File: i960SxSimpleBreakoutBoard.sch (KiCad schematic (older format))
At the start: 24 parts, among them J1 Conn_01x18, J4 Conn_01x05, J5 Multiplexed Address/Data Lines, J6 Upper 16 Address Lines, U1 80960Sx

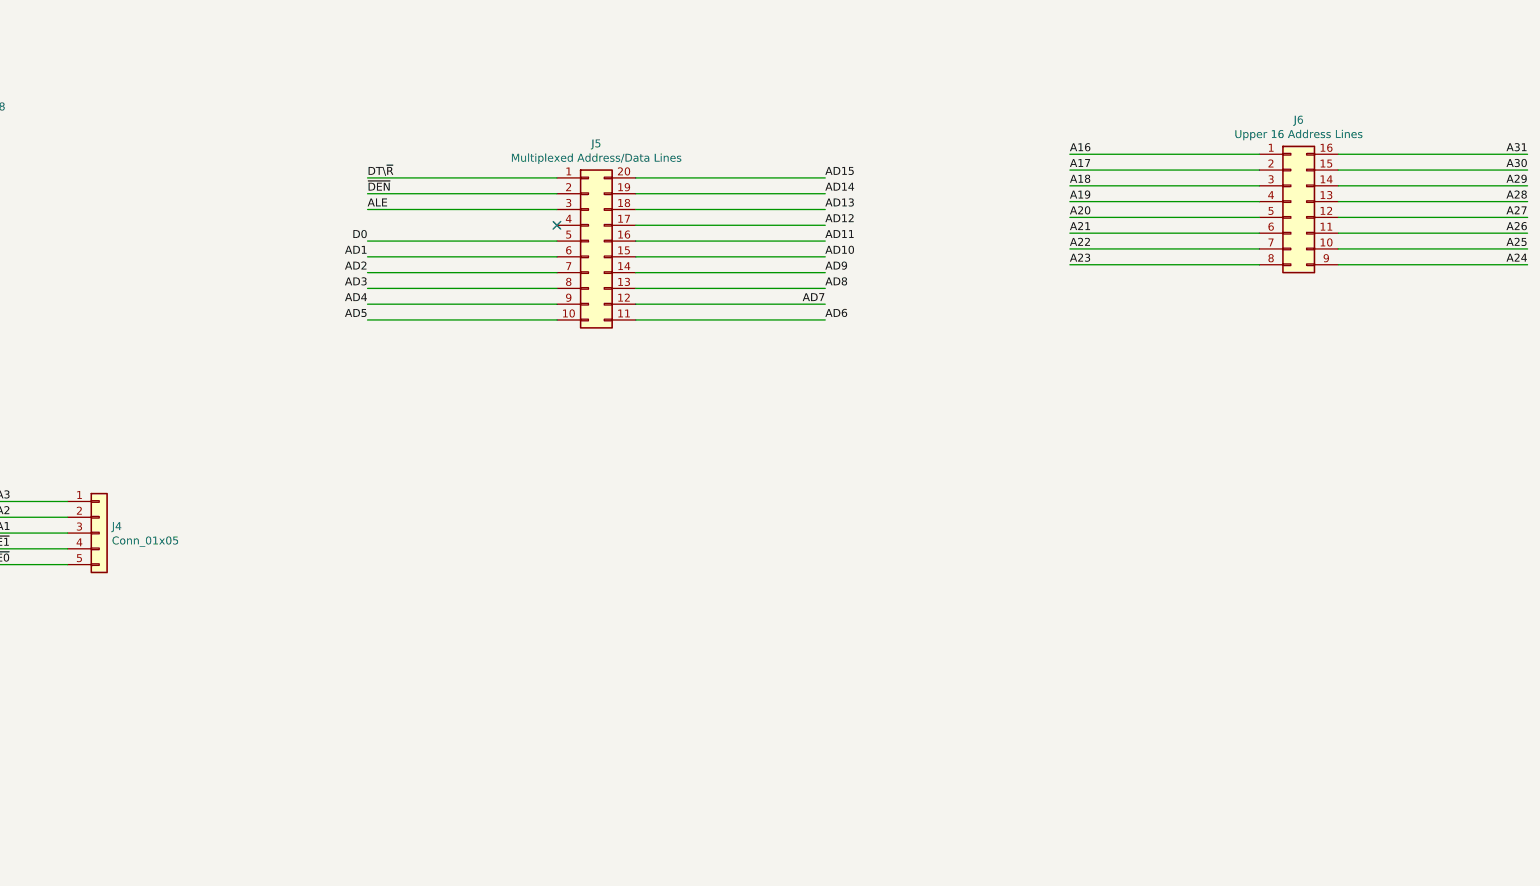
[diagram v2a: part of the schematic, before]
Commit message: Merge upper and lower address/data lines pin headers into a single 02x19 header layout
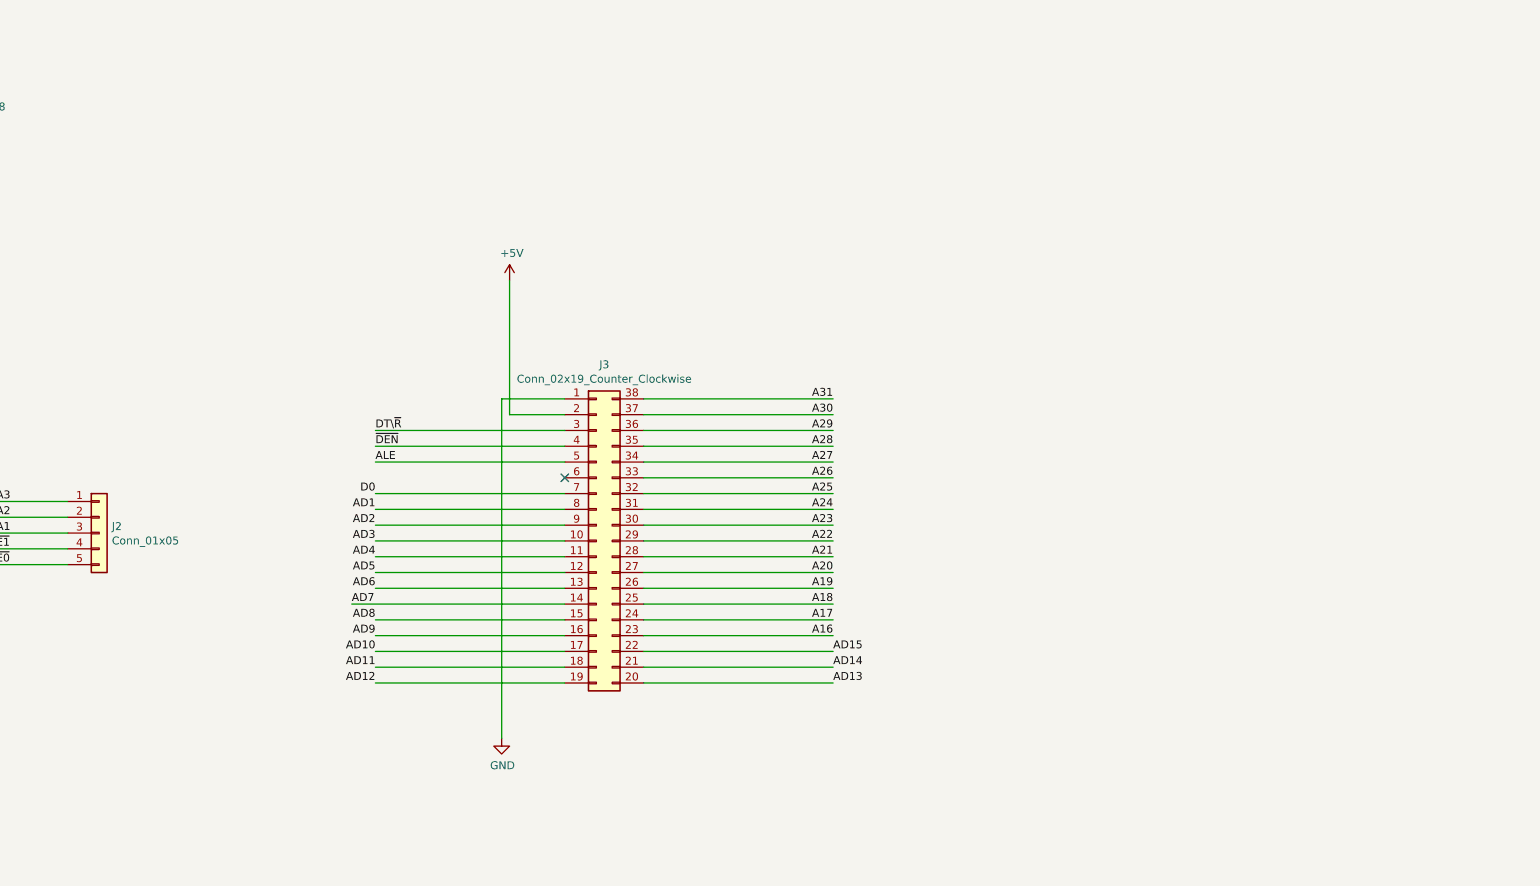
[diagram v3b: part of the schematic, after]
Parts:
- removed J5: Multiplexed Address/Data Lines, Connector_PinHeader_2.54mm:PinHeader_2x10_P2.54mm_Vertical, symbol Connector_Generic:Conn_02x10_Counter_Clockwise
- removed J6: Upper 16 Address Lines, Connector_PinHeader_2.54mm:PinHeader_2x08_P2.54mm_Vertical, symbol Connector_Generic:Conn_02x08_Counter_Clockwise
- added J3: Conn_02x19_Counter_Clockwise, Connector_PinHeader_2.54mm:PinHeader_2x19_P2.54mm_Vertical, symbol Connector_Generic:Conn_02x19_Counter_Clockwise
- renumbered J4 to J2
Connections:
- net +5V: now also J3.2 (Pin_2)
- net A16: now also J3.23 (Pin_23)
- net A17: now also J3.24 (Pin_24)
- net A18: now also J3.25 (Pin_25)
- net A19: now also J3.26 (Pin_26)
- net A20: now also J3.27 (Pin_27)
- net A21: now also J3.28 (Pin_28)
- net A22: now also J3.29 (Pin_29)
- net A23: now also J3.30 (Pin_30)
- net A24: now also J3.31 (Pin_31)
- net A25: now also J3.32 (Pin_32)
- net A26: now also J3.33 (Pin_33)
- net A27: now also J3.34 (Pin_34)
- net A28: now also J3.35 (Pin_35)
- net A29: now also J3.36 (Pin_36)
- net A30: now also J3.37 (Pin_37)
- net A31: now also J3.38 (Pin_38)
- net AD1: now also J3.8 (Pin_8)
- net AD10: now also J3.17 (Pin_17)
- net AD11: now also J3.18 (Pin_18)
- net AD12: now also J3.19 (Pin_19)
- net AD13: now also J3.20 (Pin_20)
- net AD14: now also J3.21 (Pin_21)
- net AD15: now also J3.22 (Pin_22)
- net AD2: now also J3.9 (Pin_9)
- net AD3: now also J3.10 (Pin_10)
- net AD4: now also J3.11 (Pin_11)
- net AD5: now also J3.12 (Pin_12)
- net AD6: now also J3.13 (Pin_13)
- net AD7: now also J3.14 (Pin_14)
- net AD8: now also J3.15 (Pin_15)
- net AD9: now also J3.16 (Pin_16)
- net ALE: now also J3.5 (Pin_5)
- net D0: now also J3.7 (Pin_7)
- net DT\~R: now also J3.3 (Pin_3)
- net GND: now also J3.1 (Pin_1)
- net ~DEN: now also J3.4 (Pin_4)
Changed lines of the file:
@@
 Connection ~ 7000 5050
 Wire Wire Line
-	18400 3550 17200 3550
-Wire Wire Line
-	17200 3450 18400 3450
-Wire Wire Line
-	18400 3350 17200 3350
-Wire Wire Line
-	17200 3250 18400 3250
-Wire Wire Line
-	18400 3150 17200 3150
-Wire Wire Line
-	17200 3050 18400 3050
-Wire Wire Line
-	17200 3650 18400 3650
-Wire Wire Line
-	18400 3750 17200 3750
-Wire Wire Line
-	20100 3750 18900 3750
-Wire Wire Line
-	18900 3650 20100 3650
-Wire Wire Line
-	20100 3550 18900 3550
-Wire Wire Line
-	18900 3450 20100 3450
-Wire Wire Line
-	20100 3350 18900 3350
-Wire Wire Line
-	18900 3250 20100 3250
-Wire Wire Line
-	20100 3150 18900 3150
-Wire Wire Line
-	18900 3050 20100 3050
-Text Label 20100 3050 2    50   ~ 0
+	14500 5600 15700 5600
+Wire Wire Line
+	15700 5700 14500 5700
+Wire Wire Line
+	14500 5800 15700 5800
+Wire Wire Line
+	15700 5900 14500 5900
+Wire Wire Line
+	14500 6000 15700 6000
+Wire Wire Line
+	15700 6100 14500 6100
+Wire Wire Line
+	15700 5500 14500 5500
+Wire Wire Line
+	14500 5400 15700 5400
+Wire Wire Line
+	15700 5300 14500 5300
+Wire Wire Line
+	14500 5200 15700 5200
+Wire Wire Line
+	15700 5100 14500 5100
+Wire Wire Line
+	14500 5000 15700 5000
+Wire Wire Line
+	15700 4900 14500 4900
+Wire Wire Line
+	14500 4800 15700 4800
+Wire Wire Line
+	15700 4700 14500 4700
+Wire Wire Line
+	14500 4600 15700 4600
+Text Label 15700 4600 2    50   ~ 0
 A31
-Text Label 20100 3150 2    50   ~ 0
+Text Label 15700 4700 2    50   ~ 0
 A30
-Text Label 20100 3250 2    50   ~ 0
+Text Label 15700 4800 2    50   ~ 0
 A29
-Text Label 20100 3350 2    50   ~ 0
+Text Label 15700 4900 2    50   ~ 0
 A28
-Text Label 20100 3450 2    50   ~ 0
+Text Label 15700 5000 2    50   ~ 0
 A27
-Text Label 20100 3550 2    50   ~ 0
+Text Label 15700 5100 2    50   ~ 0
 A26
-Text Label 20100 3650 2    50   ~ 0
+Text Label 15700 5200 2    50   ~ 0
 A25
-Text Label 20100 3750 2    50   ~ 0
+Text Label 15700 5300 2    50   ~ 0
 A24
-Text Label 17200 3750 0    50   ~ 0
+Text Label 15700 5400 2    50   ~ 0
 A23
-Text Label 17200 3650 0    50   ~ 0
+Text Label 15700 5500 2    50   ~ 0
 A22
-Text Label 17200 3550 0    50   ~ 0
+Text Label 15700 5600 2    50   ~ 0
 A21
-Text Label 17200 3450 0    50   ~ 0
+Text Label 15700 5700 2    50   ~ 0
 A20
-Text Label 17200 3350 0    50   ~ 0
+Text Label 15700 5800 2    50   ~ 0
 A19
-Text Label 17200 3250 0    50   ~ 0
+Text Label 15700 5900 2    50   ~ 0
 A18
-Text Label 17200 3150 0    50   ~ 0
+Text Label 15700 6000 2    50   ~ 0
 A17
-Text Label 17200 3050 0    50   ~ 0
+Text Label 15700 6100 2    50   ~ 0
 A16
 Wire Wire Line
-	13950 3300 12750 3300
-Wire Wire Line
-	12750 3600 13950 3600
-Wire Wire Line
-	13950 3700 12750 3700
-Wire Wire Line
-	12750 3800 13950 3800
-Wire Wire Line
-	13950 3900 12750 3900
-Wire Wire Line
-	12750 4000 13950 4000
-Wire Wire Line
-	13950 4100 12750 4100
+	14000 4900 12800 4900
+Wire Wire Line
+	12800 5200 14000 5200
+Wire Wire Line
+	14000 5300 12800 5300
+Wire Wire Line
+	12800 5400 14000 5400
+Wire Wire Line
+	14000 5500 12800 5500
+Wire Wire Line
+	12800 5600 14000 5600
+Wire Wire Line
+	14000 5700 12800 5700
 Text Label 3450 1850 2    50   ~ 0
 A31
@@
 Text Label 3450 3350 2    50   ~ 0
 A16
-Text Label 12750 3700 2    50   ~ 0
+Text Label 12800 5300 2    50   ~ 0
 AD1
-Text Label 12750 3800 2    50   ~ 0
+Text Label 12800 5400 2    50   ~ 0
 AD2
-Text Label 12750 3900 2    50   ~ 0
+Text Label 12800 5500 2    50   ~ 0
 AD3
-Text Label 12750 4000 2    50   ~ 0
+Text Label 12800 5600 2    50   ~ 0
 AD4
-Text Label 12750 4100 2    50   ~ 0
+Text Label 12800 5700 2    50   ~ 0
 AD5
-Text Label 15650 4100 0    50   ~ 0
+Text Label 12800 5800 2    50   ~ 0
 AD6
 Text Label 10350 5350 0    50   ~ 0
@@
 $EndComp
 Wire Wire Line
-	12750 3200 13950 3200
-Text Label 12750 3600 2    50   ~ 0
+	12800 4800 14000 4800
+Text Label 12800 5200 2    50   ~ 0
 D0
 Wire Wire Line
 	9150 3450 9150 3900
 Wire Wire Line
-	13950 3400 12750 3400
-Text Label 12750 3400 0    50   ~ 0
+	14000 5000 12800 5000
+Text Label 12800 5000 0    50   ~ 0
 ALE
 Wire Wire Line
-	15650 4100 14450 4100
-Text Label 12750 3300 0    50   ~ 0
+	12800 5800 14000 5800
+Text Label 12800 4900 0    50   ~ 0
 ~DEN
-Text Label 12750 3200 0    50   ~ 0
+Text Label 12800 4800 0    50   ~ 0
 DT\~R
 Text Label 10350 5650 0    50   ~ 0
@@
 	10350 5550 10850 5550
 $Comp
-L Connector_Generic:Conn_01x05 J4
+L Connector_Generic:Conn_01x05 J2
 U 1 1 5F839CFF
 P 11050 5450
-F 0 "J4" H 11130 5492 50  0000 L CNN
+F 0 "J2" H 11130 5492 50  0000 L CNN
 F 1 "Conn_01x05" H 11130 5401 50  0000 L CNN
 F 2 "Connector_PinHeader_2.54mm:PinHeader_1x05_P2.54mm_Vertical" H 11050 5450 50  0001 C CNN
@@
 Wire Wire Line
 	5550 7500 4850 7500
-Wire Wire Line
-	14450 4000 15650 4000
-Text Label 15650 3200 0    50   ~ 0
+Text Label 15700 6200 0    50   ~ 0
 AD15
-Text Label 15650 3300 0    50   ~ 0
+Text Label 15700 6300 0    50   ~ 0
 AD14
-Text Label 15650 3400 0    50   ~ 0
+Text Label 15700 6400 0    50   ~ 0
 AD13
-Text Label 15650 3500 0    50   ~ 0
+Text Label 12800 6400 2    50   ~ 0
 AD12
-Text Label 15650 3600 0    50   ~ 0
+Text Label 12800 6300 2    50   ~ 0
 AD11
-Text Label 15650 3700 0    50   ~ 0
+Text Label 12800 6200 2    50   ~ 0
 AD10
-Text Label 15650 3800 0    50   ~ 0
+Text Label 12800 6100 2    50   ~ 0
 AD9
-Text Label 15650 3900 0    50   ~ 0
+Text Label 12800 6000 2    50   ~ 0
 AD8
-Text Label 15650 4000 2    50   ~ 0
+Text Label 12650 5900 0    50   ~ 0
 AD7
 Wire Wire Line
-	14450 3200 15650 3200
-Wire Wire Line
-	15650 3300 14450 3300
-Wire Wire Line
-	14450 3400 15650 3400
-Wire Wire Line
-	15650 3500 14450 3500
-Wire Wire Line
-	14450 3600 15650 3600
-Wire Wire Line
-	15650 3700 14450 3700
-Wire Wire Line
-	14450 3800 15650 3800
-Wire Wire Line
-	15650 3900 14450 3900
+	14500 6200 15700 6200
+Wire Wire Line
+	15700 6300 14500 6300
+Wire Wire Line
+	14500 6400 15700 6400
+Wire Wire Line
+	12800 6400 14000 6400
+Wire Wire Line
+	14000 6300 12800 6300
+Wire Wire Line
+	12800 6200 14000 6200
+Wire Wire Line
+	14000 6100 12800 6100
+Wire Wire Line
+	12800 6000 14000 6000
 $Comp
 L Device:LED D1
@@
 	1    0    0    -1
 $EndComp
-$Comp
-L Connector_Generic:Conn_02x10_Counter_Clockwise J5
-U 1 1 5FAE9B72
-P 14150 3600
-F 0 "J5" H 14200 4217 50  0000 C CNN
-F 1 "Multiplexed Address/Data Lines" H 14200 4126 50  0000 C CNN
-F 2 "Connector_PinHeader_2.54mm:PinHeader_2x10_P2.54mm_Vertical" H 14150 3600 50  0001 C CNN
-F 3 "~" H 14150 3600 50  0001 C CNN
-	1    14150 3600
-	1    0    0    -1
-$EndComp
-$Comp
-L Connector_Generic:Conn_02x08_Counter_Clockwise J6
-U 1 1 5FB3656E
-P 18600 3350
-F 0 "J6" H 18650 3867 50  0000 C CNN
-F 1 "Upper 16 Address Lines" H 18650 3776 50  0000 C CNN
-F 2 "Connector_PinHeader_2.54mm:PinHeader_2x08_P2.54mm_Vertical" H 18600 3350 50  0001 C CNN
-F 3 "~" H 18600 3350 50  0001 C CNN
-	1    18600 3350
-	1    0    0    -1
-$EndComp
-NoConn ~ 13950 3500
 Wire Wire Line
 	9250 2850 9750 2850
@@
 	1    0    0    -1
 $EndComp
+Wire Wire Line
+	12650 5900 14000 5900
+$Comp
+L power:+5V #PWR09
+U 1 1 5FD53B4B
+P 13650 3850
+F 0 "#PWR09" H 13650 3700 50  0001 C CNN
+F 1 "+5V" H 13665 4023 50  0000 C CNN
+F 2 "" H 13650 3850 50  0001 C CNN
+F 3 "" H 13650 3850 50  0001 C CNN
+	1    13650 3850
+	1    0    0    -1
+$EndComp
+$Comp
+L power:GND #PWR010
+U 1 1 5FD61A40
+P 13600 6750
+F 0 "#PWR010" H 13600 6500 50  0001 C CNN
+F 1 "GND" H 13605 6577 50  0000 C CNN
+F 2 "" H 13600 6750 50  0001 C CNN
+F 3 "" H 13600 6750 50  0001 C CNN
+	1    13600 6750
+	1    0    0    -1
+$EndComp
+Wire Wire Line
+	14000 4600 13600 4600
+Wire Wire Line
+	13600 4600 13600 6750
+Wire Wire Line
+	14000 4700 13650 4700
+Wire Wire Line
+	13650 4700 13650 3850
+$Comp
+L Connector_Generic:Conn_02x19_Counter_Clockwise J3
+U 1 1 5FE50A31
+P 14200 5500
+F 0 "J3" H 14250 6617 50  0000 C CNN
+F 1 "Conn_02x19_Counter_Clockwise" H 14250 6526 50  0000 C CNN
+F 2 "Connector_PinHeader_2.54mm:PinHeader_2x19_P2.54mm_Vertical" H 14200 5500 50  0001 C CNN
+F 3 "~" H 14200 5500 50  0001 C CNN
+	1    14200 5500
+	1    0    0    -1
+$EndComp
+NoConn ~ 14000 5100
 $EndSCHEMATC
